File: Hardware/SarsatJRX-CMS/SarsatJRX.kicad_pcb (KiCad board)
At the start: 2 copper layers, 65 x 56.5 mm, 60 parts, among them J3 LilyPi GPIO Header, Q1 S8050, U1 TLC2274, U2 TLC2274

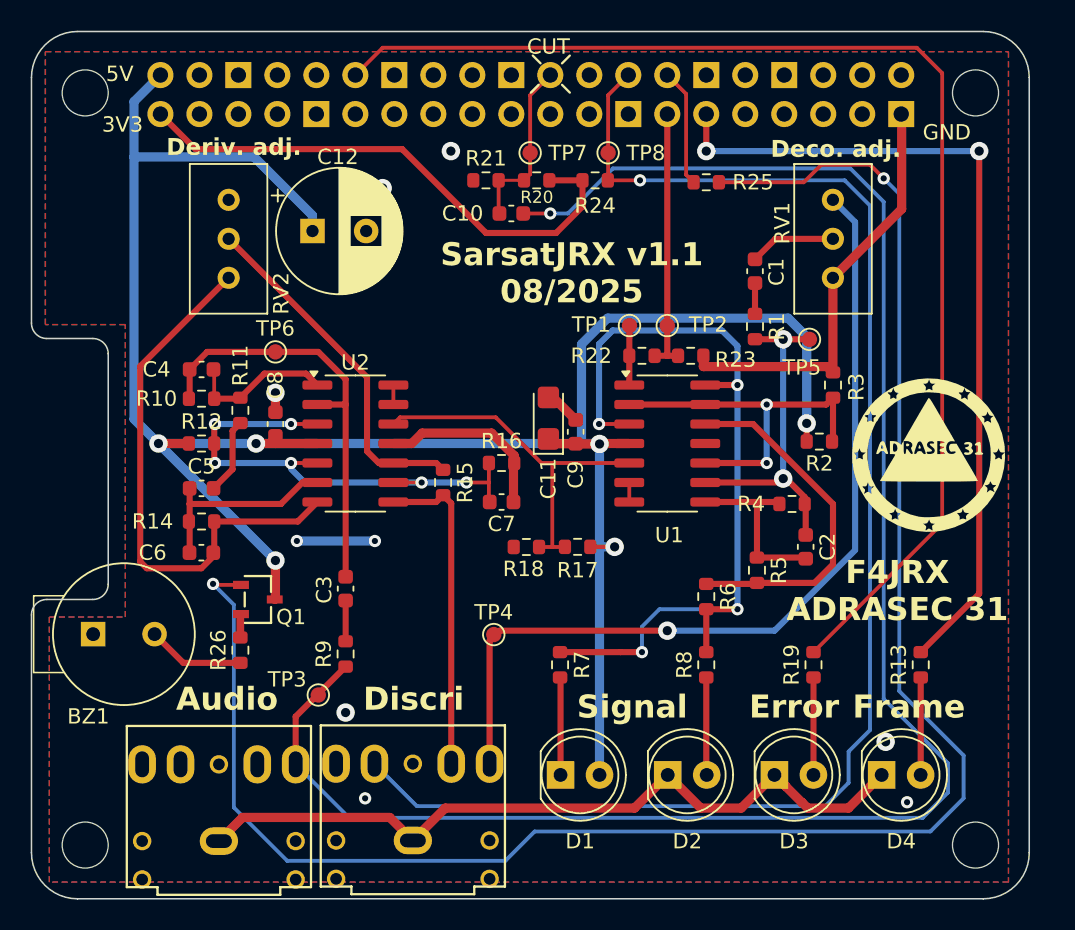
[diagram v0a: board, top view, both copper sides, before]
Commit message: Fixed 5V line capacitor value (3300uF) + footprint. Added decoupling capacitor to U2 power line. Added RV1/2 value sikl screen. Added slik screen to mark connector pins that have to be soldered. Moved to v1.2.
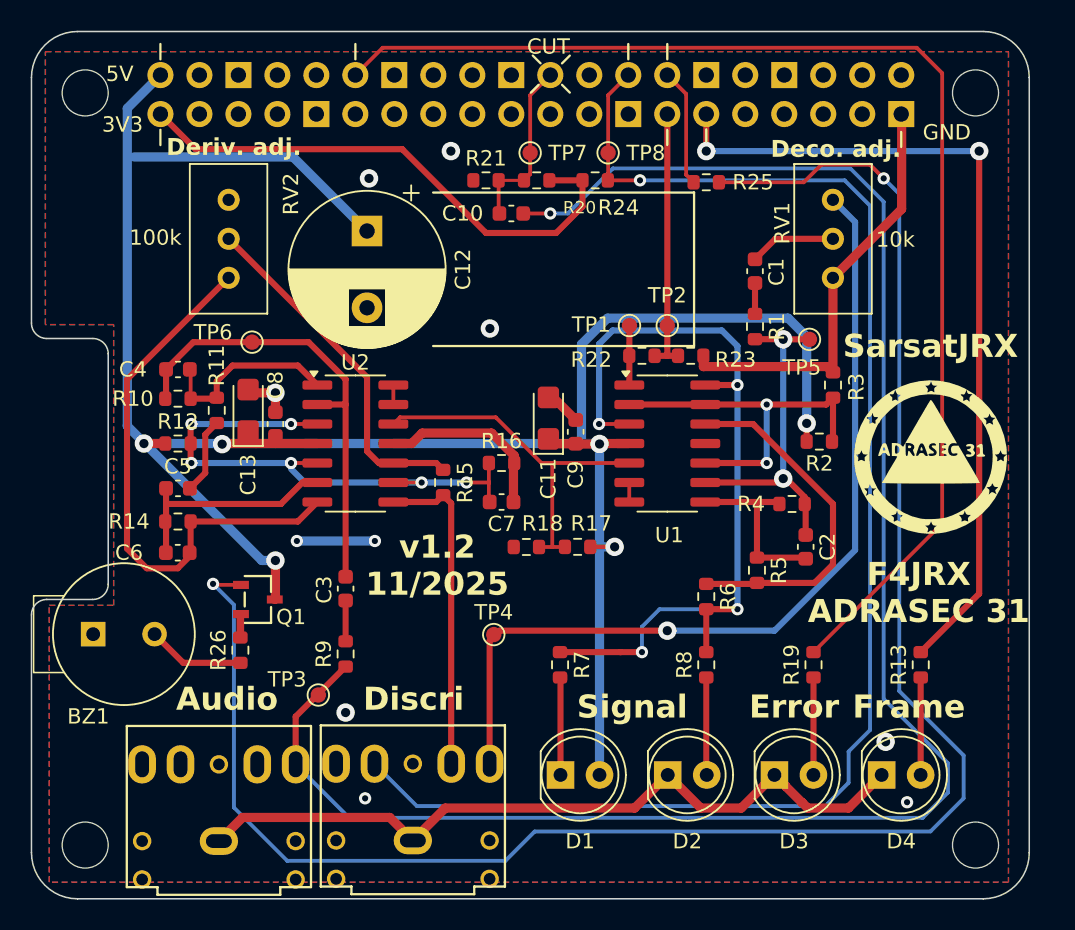
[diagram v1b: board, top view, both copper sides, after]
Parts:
- added C13: 10uF, Capacitor_Tantalum_SMD:CP_EIA-3216-18_Kemet-A, F.Cu at (126.5, 85.8)
- C12: value 470uF -> 3300uF; footprint Capacitor_THT:CP_Radial_D8.0mm_P3.50mm -> Capacitor_THT:CP_Radial_D10.0mm_P5.00mm
- moved C12 3.56 mm to (134.2, 74.2), turned to -90 degrees
- moved TP6 1.65 mm to (126.7, 81.4)
- moved C4 1.54 mm to (121.9, 83.2)
- moved C5 1.54 mm to (121.9, 90.9)
- moved R10 1.54 mm to (121.9, 85.1)
- moved R11 1.54 mm to (124.4, 85.8)
- moved R12 1.54 mm to (121.9, 88.0)
- moved R14 1.54 mm to (121.9, 93.1)
- moved C6 1.54 mm to (121.9, 95.1)
- moved G*** 0.18 mm to (170.9, 88.9)
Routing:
- net +5V: track 146.9 -> 153.4 mm
- net Net-(U2A-+): track 34.0 -> 37.0 mm
- net Net-(C4-Pad2): track 9.64 -> 12.2 mm
- net Net-(U2A--): track 28.0 -> 30.1 mm
- net GND: track 98.3 -> 100.2 mm
- net Net-(U2B--): track 13.0 -> 14.5 mm
- net Net-(C6-Pad2): track 35.7 -> 36.4 mm
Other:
- board text added: "100k"
- board text added: "10k"
- board text added: "SarsatJRX"
- board text added: "v1.2 11/2025"
- board text removed: "SarsatJRX v1.1 08/2025"
